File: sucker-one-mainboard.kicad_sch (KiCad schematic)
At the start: 120 parts, among them J1 JST NC Valve, J10 JST Motor, J11 Conn_02x04_Odd_Even, J12 TYPE-C-31-M-12, J2 JST NO Valve, J3 6P4C, J4 JST 3 Way Valve, J5 Jack-DC, J6 Phoenix Contact 1733570, J7 QWIIC I2C, J8 SPI, J9 52271-1079, Q1 BSS138, Q2 BSS138, Q3 BSS138, Q6 STN4NF20L, U1 LD1117S33TR, Y1 ABLS-12.000MHZ-B4-T

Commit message: Cleanup
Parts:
- removed C1: 1u, Capacitor_SMD:C_0603_1608Metric_Pad1.08x0.95mm_HandSolder, symbol Device:C
- removed C10, C13, C14, C2, C5: 100n, Capacitor_SMD:C_0603_1608Metric_Pad1.08x0.95mm_HandSolder, symbol Device:C
- removed FB1: Ferrite_Bead, Inductor_SMD:L_0603_1608Metric_Pad1.05x0.95mm_HandSolder, symbol sucker-one-mainboard-rescue:Ferrite_Bead-Device
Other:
- note added: "Expansion Port Test Pins"
- note removed: "Decoupling & Filtering"
- moved on the sheet: C21, C6, C7, C?, D10, D11, D2, D3, D7, D8, D9, J1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

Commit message: Assign or update remaining footprints
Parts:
- C1, C2, C4, C5, C8, C9: renamed from C?; footprint Capacitor_SMD:C_0603_1608Metric_Pad1.08x0.95mm_HandSolder -> Capacitor_SMD:C_0603_1608Metric
- C10, C12, C13, C14, C15, C16, C17, C18, C19, C20, C22, C23: renamed from C?; footprint Capacitor_SMD:C_0603_1608Metric_Pad1.08x0.95mm_HandSolder -> Capacitor_SMD:C_0402_1005Metric
- C11, C3, C6, C7: footprint Capacitor_SMD:C_0603_1608Metric_Pad1.08x0.95mm_HandSolder -> Capacitor_SMD:C_0603_1608Metric
- L1: renamed from L?; value 4.7uH -> VLS6045EX-4R7M 4.7uH; Source https://lcsc.com/product-detail/Power-Inductors_SXN-Shun-Xi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 -> https://lcsc.com/product-detail/Power-Inductors_TDK-VLS6045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
- SW1: renamed from SW?; footprint (none) -> Button_Switch_THT:SW_Tactile_SKHH_Angled
- U2: renamed from U?; footprint SOT95P280X110-6N -> TPS561201DDCR:SOT95P280X110-6N
- U4: renamed from U?; footprint RP2040_minimal:RP2040-QFN-56 -> RP2040:RP2040-QFN-56
- Y1: footprint (none) -> ABLS-12:XTAL_ABLS-8.000MHZ-B2-T
- gave numbers to parts that had none: 9
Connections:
- net SPI1_CS is gone; now on net SPI0_CS: U4.32 (GPIO21)
- net +1V1: now also C12.2

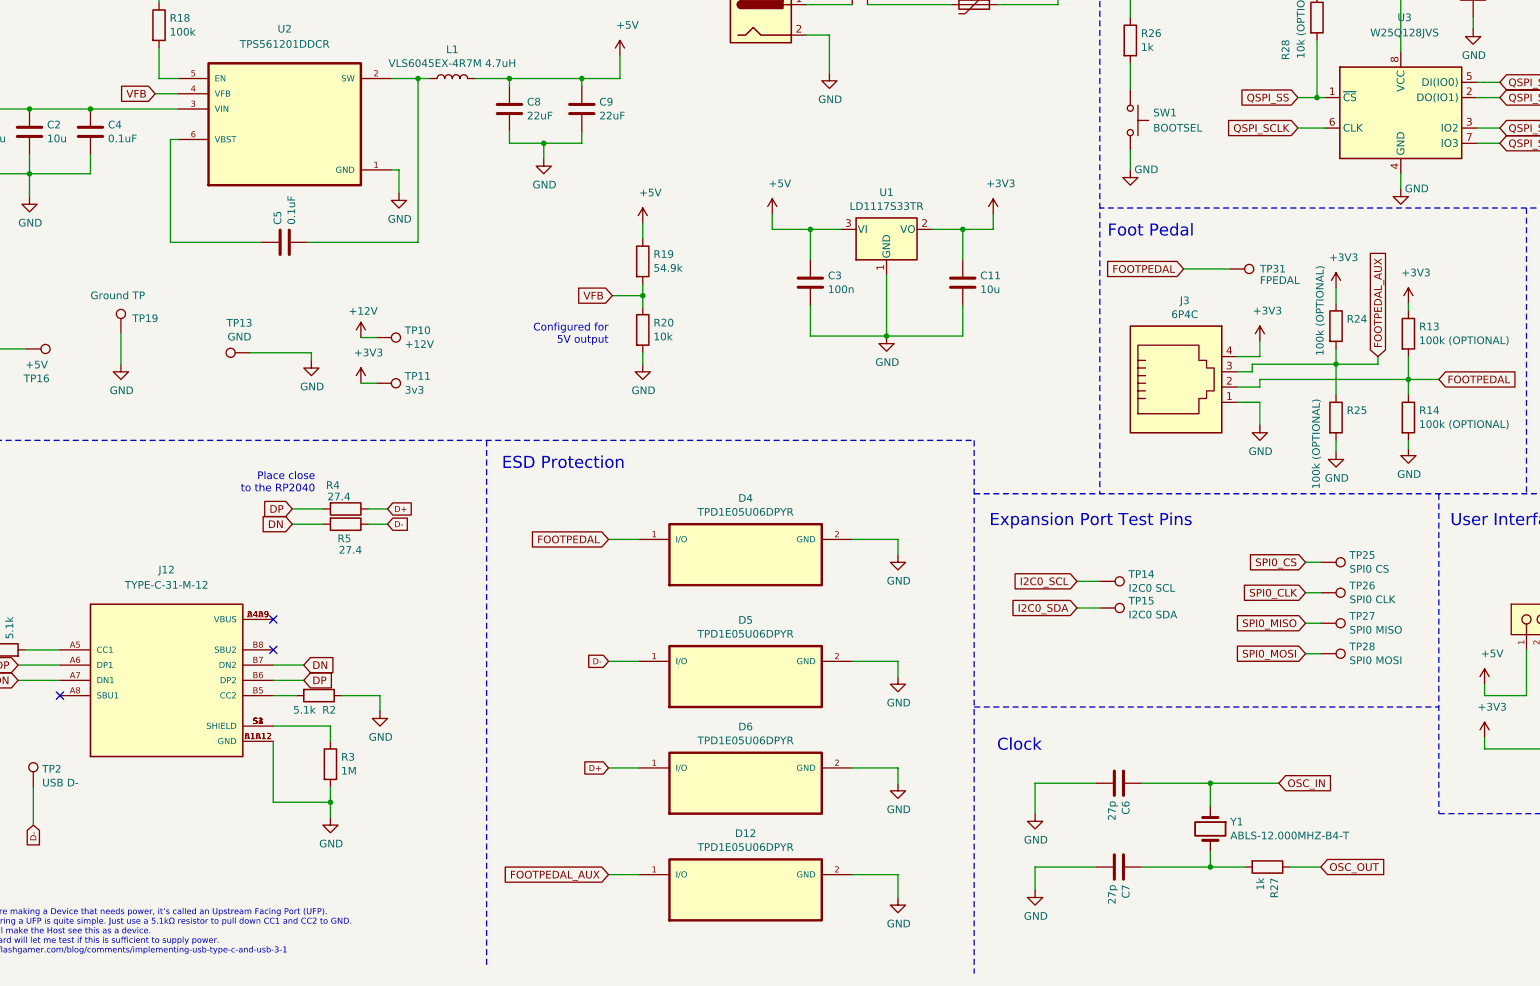
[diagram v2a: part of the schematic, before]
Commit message: Update crystal and footprints of components
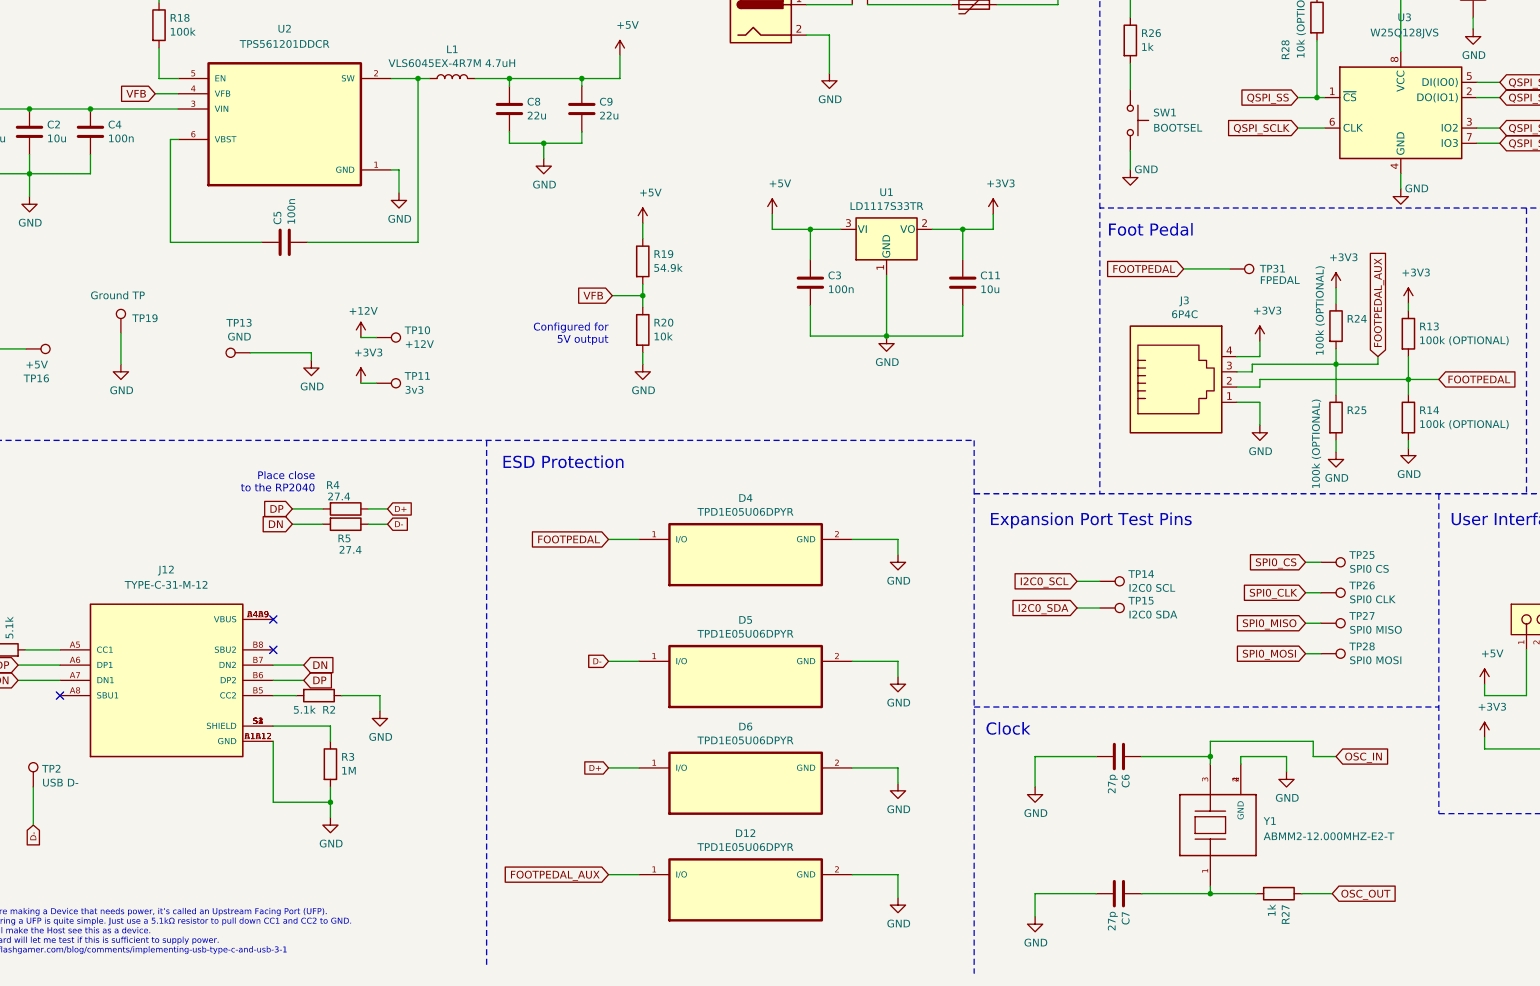
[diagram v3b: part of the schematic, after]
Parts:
- removed Y1: ABLS-12.000MHZ-B4-T, ABLS-12:XTAL_ABLS-8.000MHZ-B2-T, symbol Device:Crystal
- added Y1: ABMM2-12.000MHZ-E2-T, ABMM2-12:XTAL_ABMM2-12.000MHZ-E2-T, symbol ABMM2-12.000MHZ-E2-T:ABMM2-12.000MHZ-E2-T
- C4, C5: value 0.1uF -> 100n
- C8, C9: value 22uF -> 22u
- D2, D7, D8: footprint LED_SMD:LED_0603_1608Metric_Pad1.05x0.95mm_HandSolder -> LED_SMD:LED_0603_1608Metric
- F1: footprint Fuse:Fuse_1812_4532Metric_Pad1.30x3.40mm_HandSolder -> Fuse:Fuse_1812_4532Metric
- R1, R10, R11, R12, R13, R14, R15, R16, R17, R18, R19, R2, R20, R21, R22, R23, R24, R25, R26, R27, R28, R3, R6, R7, R8, R9: footprint Resistor_SMD:R_0603_1608Metric_Pad0.98x0.95mm_HandSolder -> Resistor_SMD:R_0603_1608Metric
- R4, R5: footprint Resistor_SMD:R_0603_1608Metric_Pad0.98x0.95mm_HandSolder -> Resistor_SMD:R_0402_1005Metric
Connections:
- net GND: now also Y1.2 (GND), Y1.4 (GND)
- net OSC_IN: now also Y1.3
- net at C7.1, R27.2: now also Y1.1
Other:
- moved on the sheet: C6, C7, R27

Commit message: RP2040 PCB routed
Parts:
- removed TP17: PUMP+, TestPoint:TestPoint_Pad_D2.0mm, symbol Connector:TestPoint
- removed TP3: NC+, TestPoint:TestPoint_Pad_D2.0mm, symbol Connector:TestPoint
- removed TP6: NO+, TestPoint:TestPoint_Pad_D2.0mm, symbol Connector:TestPoint
- removed TP8: 3W+, TestPoint:TestPoint_Pad_D2.0mm, symbol Connector:TestPoint
- added H1, H2, H3, H4, H5: MountingHole, MountingHole:MountingHole_3.2mm_M3_Pad_Via, symbol Mechanical:MountingHole
- added TP20: FPEDAL, TestPoint:TestPoint_Pad_D2.0mm, symbol Connector:TestPoint
- C21: value 330u 35v -> 100n 35v; footprint Capacitor_SMD:CP_Elec_10x10 -> Capacitor_Tantalum_SMD:CP_EIA-3216-18_Kemet-A; LCSC https://lcsc.com/product-detail/Aluminum-Electrolytic-Capac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 -> (none); Source (none) -> https://lcsc.com/product-detail/Tantalum-Capacitors_KEMET-T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
- U3: footprint Package_SO:SOIC-8_5.23x5.23mm_P1.27mm -> W25Q128JVPIQ:SON127P500X600X80-9N
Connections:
- net D+: no longer D6.1 (I/O), TP1.1
- net D-: no longer D5.1 (I/O), TP2.1
- net DN: now also D5.1 (I/O), TP2.1
- net DP: now also D6.1 (I/O), TP1.1
- net FOOTPEDAL_AUX: now also TP20.1
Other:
- moved on the sheet: TP31

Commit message: Change various things
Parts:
- removed C1, C2: 10u, Capacitor_SMD:C_0603_1608Metric, symbol Device:C
- removed C21: 100n 35v, Capacitor_Tantalum_SMD:CP_EIA-3216-18_Kemet-A, symbol sucker-one-mainboard-rescue:CP-Device
- removed C4, C5: 100n, Capacitor_SMD:C_0603_1608Metric, symbol Device:C
- removed C8, C9: 22u, Capacitor_SMD:C_0603_1608Metric, symbol Device:C
- removed D11: SOD4007, Diode_SMD:D_SOD-123F, symbol Device:D
- removed D12, D4, D5, D6: TPD1E05U06DPYR, TPD1E05U06DPYR:DIO_TPD1E05U06DPYR, symbol sucker-one-mainboard-rescue:TPD1E05U06DPYR-TPD1E05U06DPYR
- removed J10: JST Motor, Connector_JST:JST_XH_B2B-XH-A_1x02_P2.50mm_Vertical, symbol Connector:Conn_01x02_Male
- removed J9: 52271-1079, Molex 52271-1079:Molex-52271-1079-Manufacturer_Recommended, symbol MOLEX 10 Pin 1mm FFC con:52271-1079
- removed L1: VLS6045EX-4R7M 4.7uH, Inductor_SMD:L_Bourns_SRN6045TA, symbol Device:L
- removed Q6: STN4NF20L, STN4NF20L:SOT223, symbol STN4NF20L:STN4NF20L
- removed R14, R24, R25: 100k (OPTIONAL), Resistor_SMD:R_0603_1608Metric, symbol Device:R
- removed R16, R18: 100k, Resistor_SMD:R_0603_1608Metric, symbol Device:R
- removed R19: 54.9k, Resistor_SMD:R_0603_1608Metric, symbol Device:R
- removed R20: 10k, Resistor_SMD:R_0603_1608Metric, symbol Device:R
- removed R23: 160, Resistor_SMD:R_0603_1608Metric, symbol Device:R
- removed TP18: PUMP-, TestPoint:TestPoint_Pad_D2.0mm, symbol Connector:TestPoint
- removed U2: TPS561201DDCR, TPS561201DDCR:SOT95P280X110-6N, symbol TPS561201DDCR:TPS561201DDCR
- added C21: 1n, symbol Device:C
- added C24, C25, C26, C27: 100n, Capacitor_SMD:C_0402_1005Metric, symbol Device:C
- added C?: 22u 10v, Capacitor_SMD:C_0805_2012Metric_Pad1.18x1.45mm_HandSolder, symbol Device:C
- added C?: 3.3n 25V, Capacitor_SMD:C_0603_1608Metric_Pad1.08x0.95mm_HandSolder, symbol Device:C
- added C?: 10u 25V, Capacitor_SMD:C_1210_3225Metric_Pad1.33x2.70mm_HandSolder, symbol Device:C
- added C?: 10u 25v DNP, Capacitor_SMD:C_0603_1608Metric, symbol Device:C
- added D1, D4: SP0502BAHT, Package_TO_SOT_SMD:SOT-23, symbol Power_Protection:SP0502BAHT
- added D?: 10v 500mW DNP, symbol Device:D_Zener
- added J?: BM10B-SRSS-TB(LF)(SN), JST_BM10B-SRSS-TB(LF)(SN), symbol BM10B-SRSS-TB(LF)(SN):BM10B-SRSS-TB(LF)(SN)
- added J?: BM04B-SRSS-TBT(LF)(SN), Connector_JST:JST_SH_BM04B-SRSS-TB_1x04-1MP_P1.00mm_Vertical, symbol Connector_Generic:Conn_01x04
- added L?: 2.2uH 3.1A XFL4020-222MEB, Inductor_SMD:L_Coilcraft_XxL4020, symbol Device:L
- added Q?: STN4NF20L, STN4NF20L:SOT223, symbol STN4NF20L:STN4NF20L
- added R?: 0 DNP, Resistor_SMD:R_0805_2012Metric_Pad1.20x1.40mm_HandSolder, symbol Device:R
- added R? (x2): 220, Resistor_SMD:R_0603_1608Metric_Pad0.98x0.95mm_HandSolder, symbol Device:R
- added R?: 99.7k, Resistor_SMD:R_0603_1608Metric_Pad0.98x0.95mm_HandSolder, symbol Device:R
- added R?: 100k, Resistor_SMD:R_0603_1608Metric_Pad0.98x0.95mm_HandSolder, symbol Device:R
- added R?: 19k, Resistor_SMD:R_0603_1608Metric_Pad0.98x0.95mm_HandSolder, symbol Device:R
- added R?: 10k, Resistor_SMD:R_0603_1608Metric_Pad0.98x0.95mm_HandSolder, symbol Device:R
- added U?: TPS62143RGTT, Package_DFN_QFN:VQFN-16-1EP_3x3mm_P0.5mm_EP1.68x1.68mm_ThermalVias, symbol Regulator_Switching:TPS62143
- H1, H2, H3, H4, H5: now left out of the parts list
- J11: value Conn_02x04_Odd_Even -> UART/SWD DNP
- R13: value 100k (OPTIONAL) -> 100; footprint Resistor_SMD:R_0603_1608Metric -> (none)
- R28: value 10k (OPTIONAL) -> 10k DNP
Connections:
- net +12V: now also J6.2 (Pin_2), C?.1, J?.1 (Pin_1), U?.10 (AVIN), U?.11 (PVIN), U?.12 (PVIN), U?.13 (EN); no longer F1.1
- net +3V3: now also C25.2, C26.2, C27.2, J?.2; no longer R13.1
- net +5V: now also C24.2, C?.1, J?.1, L?.2, R?.1, R?.1, U?.14 (VOS)
- net DN: now also D4.2 (K)
- net DP: now also D4.1 (K)
- net Drop Btn: now also J?.4
- net FOOTPEDAL: now also D1.2 (K), R?.2; no longer J3.2, R13.2
- net FOOTPEDAL_AUX: now also D1.1 (K), R?.2; no longer J3.3
- net GND: now also C21.1, C24.1, C25.1, C26.1, C27.1, C?.2, C?.2, C?.2, D1.3 (A), D4.3 (A), D?.2 (A), J?.10, J?.4 (Pin_4), J?.S1 (SHIELD), J?.S2 (SHIELD), Q?.3, R?.2, R?.2, U?.15 (PGND), U?.16 (PGND), U?.6 (AGND), U?.7 (FSW), U?.8 (DEF); no longer J5.2
- net High Btn: now also J?.6
- net Lift Btn: now also J?.3
- net Low Btn: now also J?.5
- net MOTOR_PWM: now also J?.2 (Pin_2)
- net Reverse Btn: now also J?.7
- net Trigger Btn: now also J?.8
- net UI LED Data: now also R13.2
- net at J6.1 (Pin_1): now also F1.1, C?.1, R?.1; no longer J5.1
- net at F1.2: now also J5.1; no longer J6.2 (Pin_2)
- net BEMF: now reaches U4.38 (GPIO26_ADC0)
- net BEMF: now also J?.3 (Pin_3)
- net at J12.S1 (SHIELD), J12.S2 (SHIELD), J12.S3 (SHIELD)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: now also C21.2
- new net: J3.2, R?.1
- new net: J3.3, R?.1
- new net: J5.2, Q?.2, Q?.T, R?.1
- new net: J?.9, R13.1
- new net: L?.1, U?.1 (SW), U?.2 (SW), U?.3 (SW)
- new net: R?.2, U?.4 (PG)
- new net: C?.1, U?.9 (SS/TR)
- new net: C?.2, D?.1 (K), Q?.1, R?.2
- new net FB: R?.1, R?.2, U?.5 (FB)
- no-connect marks 14 -> 13
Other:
- note added: "DC MOTOR"
- note added: "REV POL PROTECT BYPASS"
- note removed: "Configured for 5V output"
- moved on the sheet: C11, C3, D2, D3, D7, D9, F1, H1, H2, H3, H4, H5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
